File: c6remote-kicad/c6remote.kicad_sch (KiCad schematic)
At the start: 25 parts, among them J1 Battery, Q1 MMBT2222A, SW1 SW_Push, SW10 SW_Push, SW11 SW_Push, SW2 SW_Push, SW3 SW_Push, SW4 SW_Push, SW5 SW_Push, SW6 SW_Push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

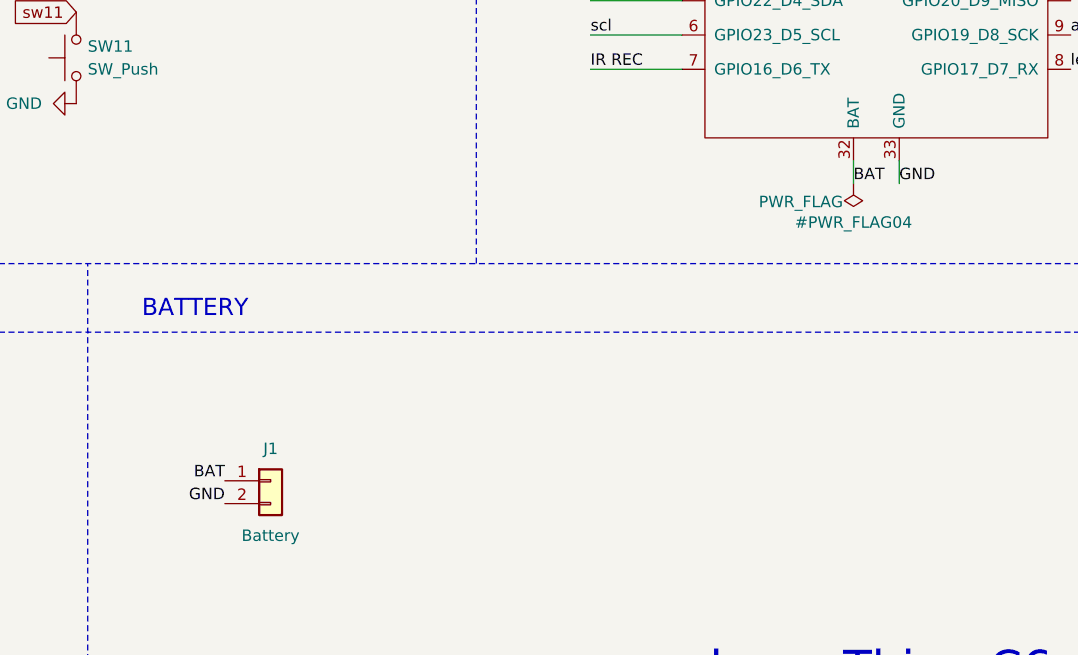
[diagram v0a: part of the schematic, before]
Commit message: fix(net): rename BAT local labels to global so net emits as 'BAT' not '/BAT'; patch stale PCB pad nets U1.32 BAT_32 and MK1.5 VDD_5 from PWR_FLAG to BAT/+3.3V; refill zones (DRC: 0 errors, 42 warnings, was 50 with 4 errors)
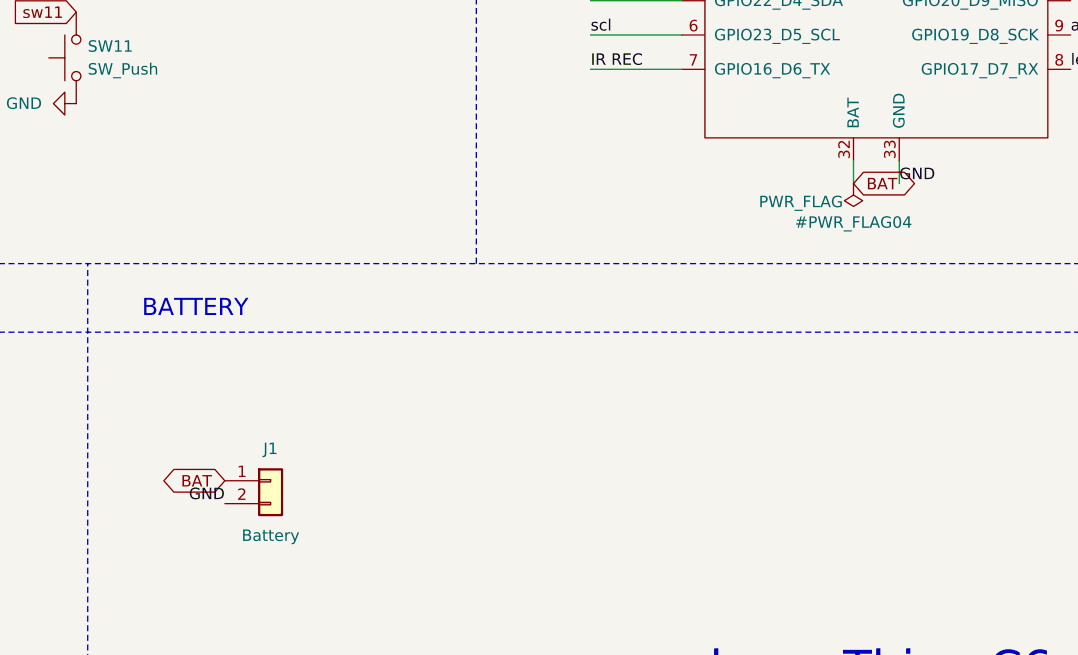
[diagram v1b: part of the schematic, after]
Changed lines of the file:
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@@
-		)
-	)
-	(label "BAT"
-		(at 128.27 153.67 180)
-		(effects
-			(font
-				(size 1.27 1.27)
-			)
-			(justify right bottom)
 		)
 	)
@@
 		)
 	)
-	(label "BAT"
-		(at 198.12 120.65 0)
-		(effects
-			(font
-				(size 1.27 1.27)
-			)
-			(justify left bottom)
-		)
-	)
 	(label "IR EMIT"
 		(at 168.91 88.9 0)
@@
 		)
 	)
+	(global_label "BAT"
+		(shape bidirectional)
+		(at 128.27 153.67 180)
+		(effects
+			(font
+				(size 1.27 1.27)
+			)
+			(justify right bottom)
+		)
+		(property "Intersheetrefs" "${INTERSHEET_REFS}"
+			(at 128.27 153.67 0)
+			(hide yes)
+			(show_name no)
+			(do_not_autoplace no)
+			(effects
+				(font
+					(size 1.27 1.27)
+				)
+			)
+		)
+	)
 	(global_label "ano_sw4"
 		(shape input)
@@
 			)
 		)
+	)
+	(global_label "BAT"
+		(shape bidirectional)
+		(at 198.12 120.65 0)
+		(effects
+			(font
+				(size 1.27 1.27)
+			)
+			(justify left bottom)
+		)
+		(property "Intersheetrefs" "${INTERSHEET_REFS}"
+			(at 198.12 120.65 0)
+			(hide yes)
+			(show_name no)
+			(do_not_autoplace no)
+			(effects
+				(font
+					(size 1.27 1.27)
+				)
+			)
+		)

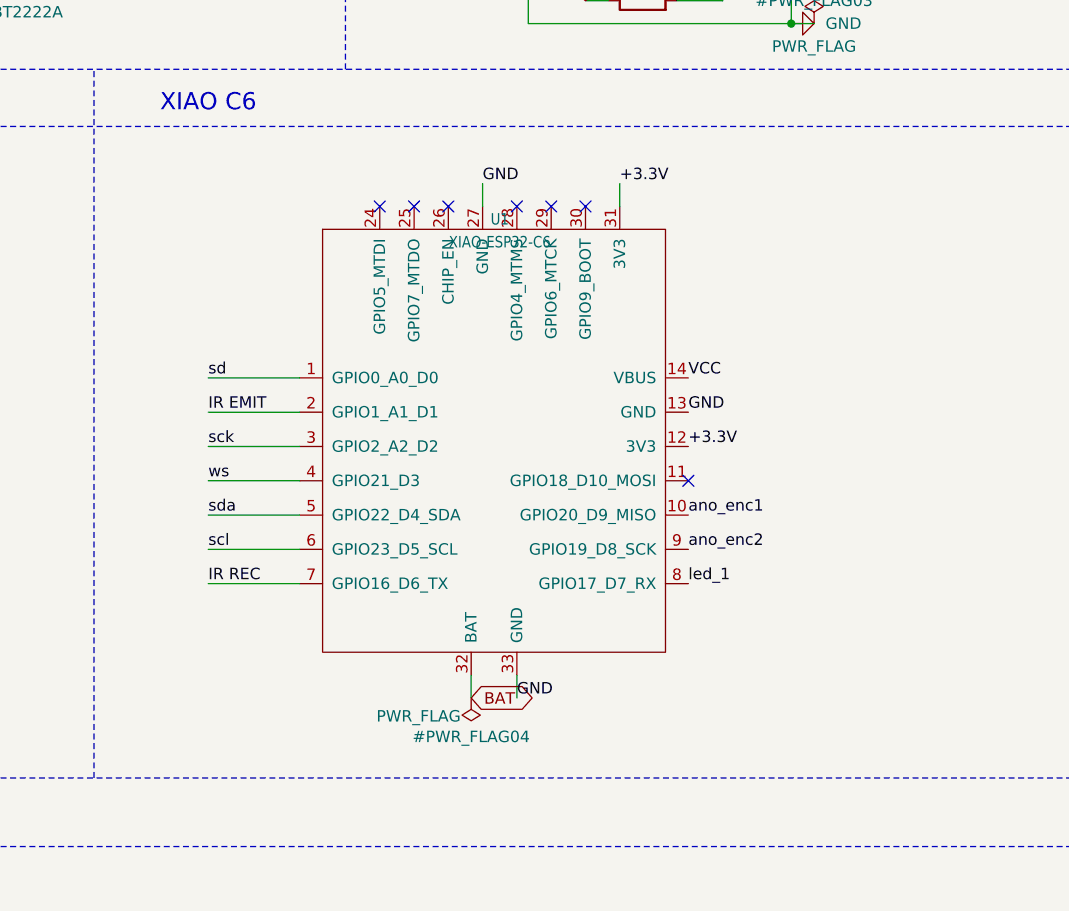
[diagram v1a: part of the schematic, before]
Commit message: feat(schematic): add I2C pull-ups R4 (4.7k SDA->+3.3V) and R5 (4.7k SCL->+3.3V) west of XIAO label bundle with shared #PWR033 +3.3V symbol; ERC clean (0 errors, 12 baseline warnings); PCB placement pending
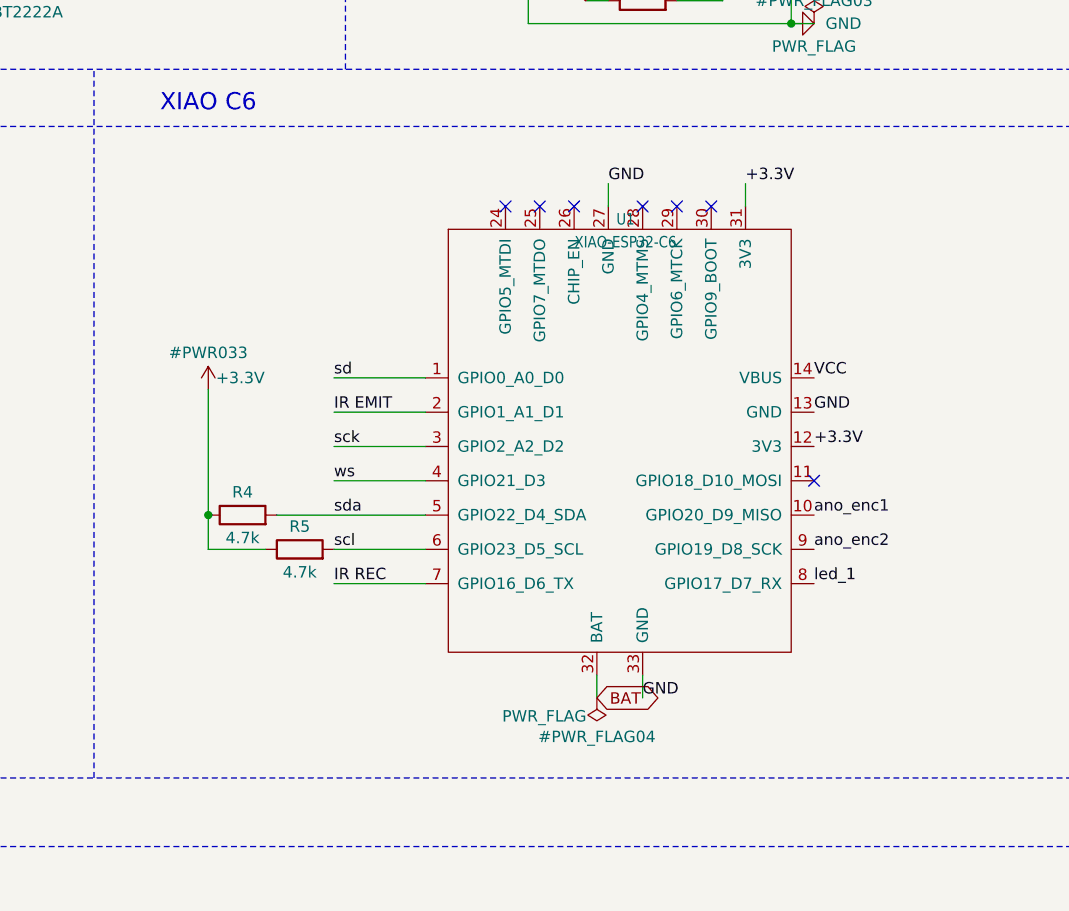
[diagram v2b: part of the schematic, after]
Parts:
- added R4, R5: 4.7k, Resistor_SMD:R_0603_1608Metric, symbol Device:R
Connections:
- net +3.3V: now also R4.1, R5.1
- net scl: now also R5.2
- net sda: now also R4.2
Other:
- moved on the sheet: U1

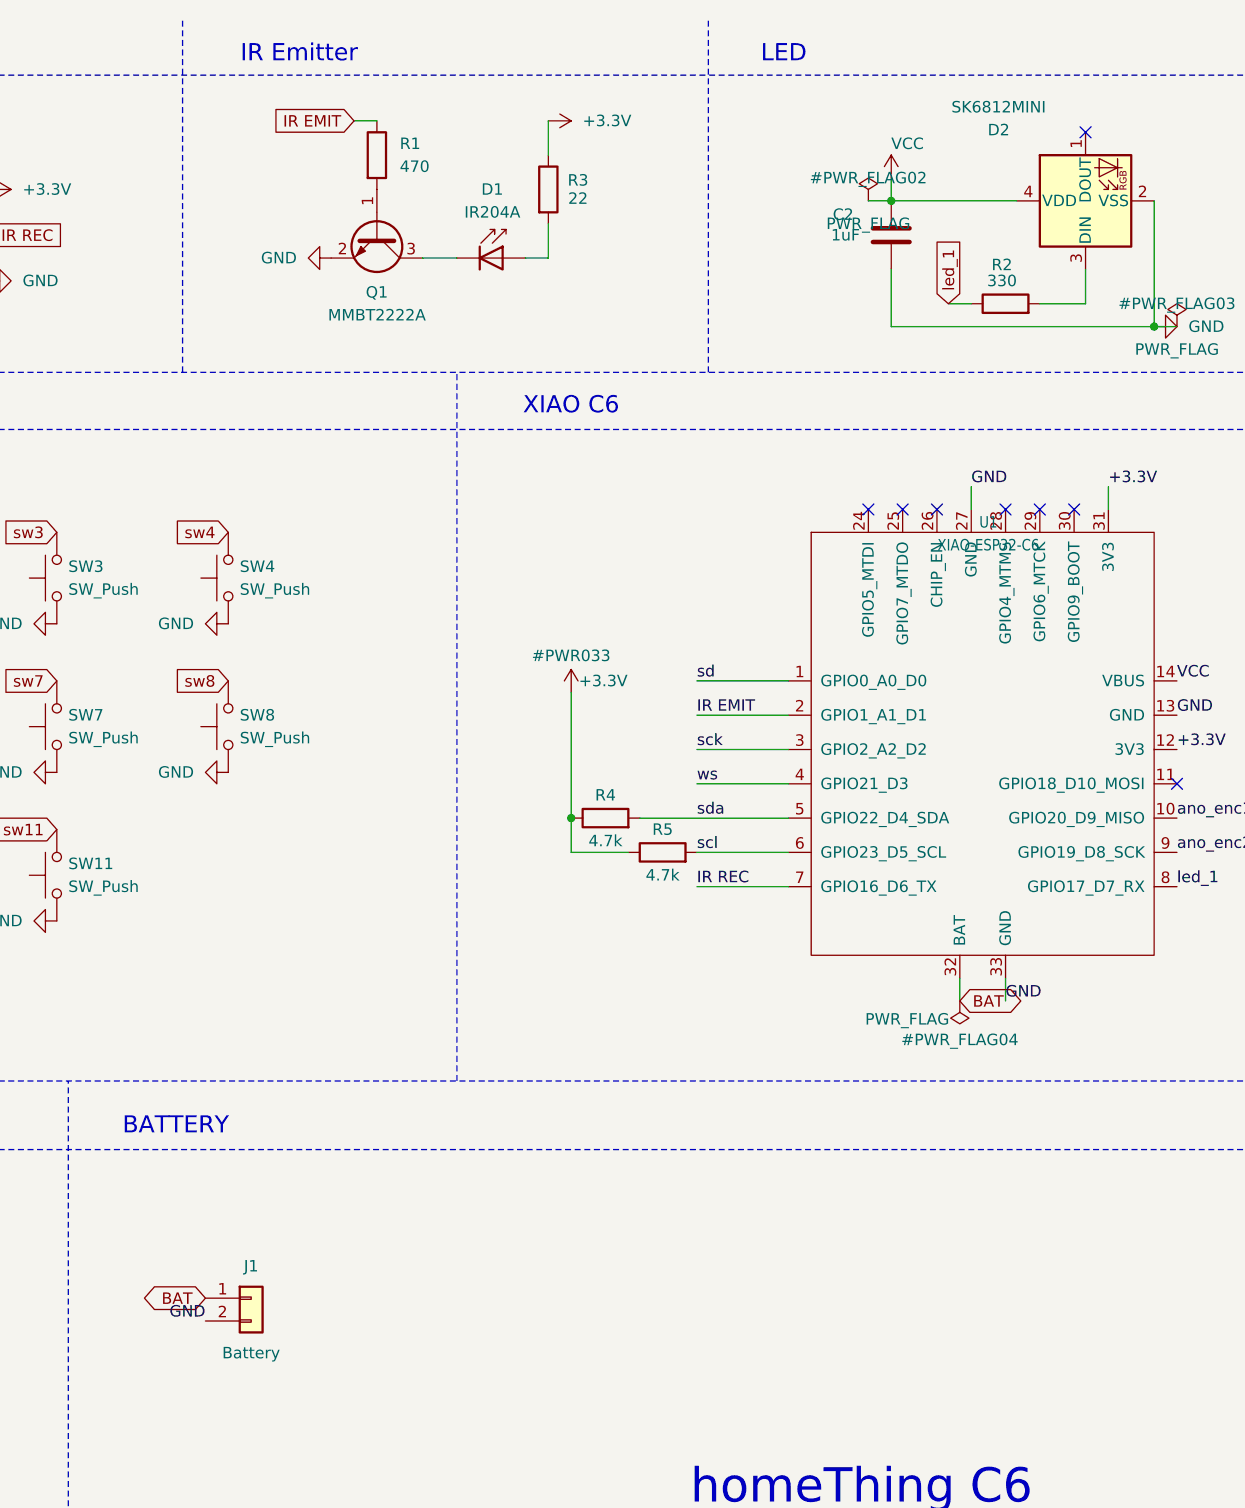
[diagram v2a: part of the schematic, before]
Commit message: fix(power): move SK6812 D2 supply from VCC (VBUS) to +3.3V so LED works on battery; rewires D2/4 + C2/1; VCC label now only U1/14 (orphan single-node /VCC net, rename to VBUS later)
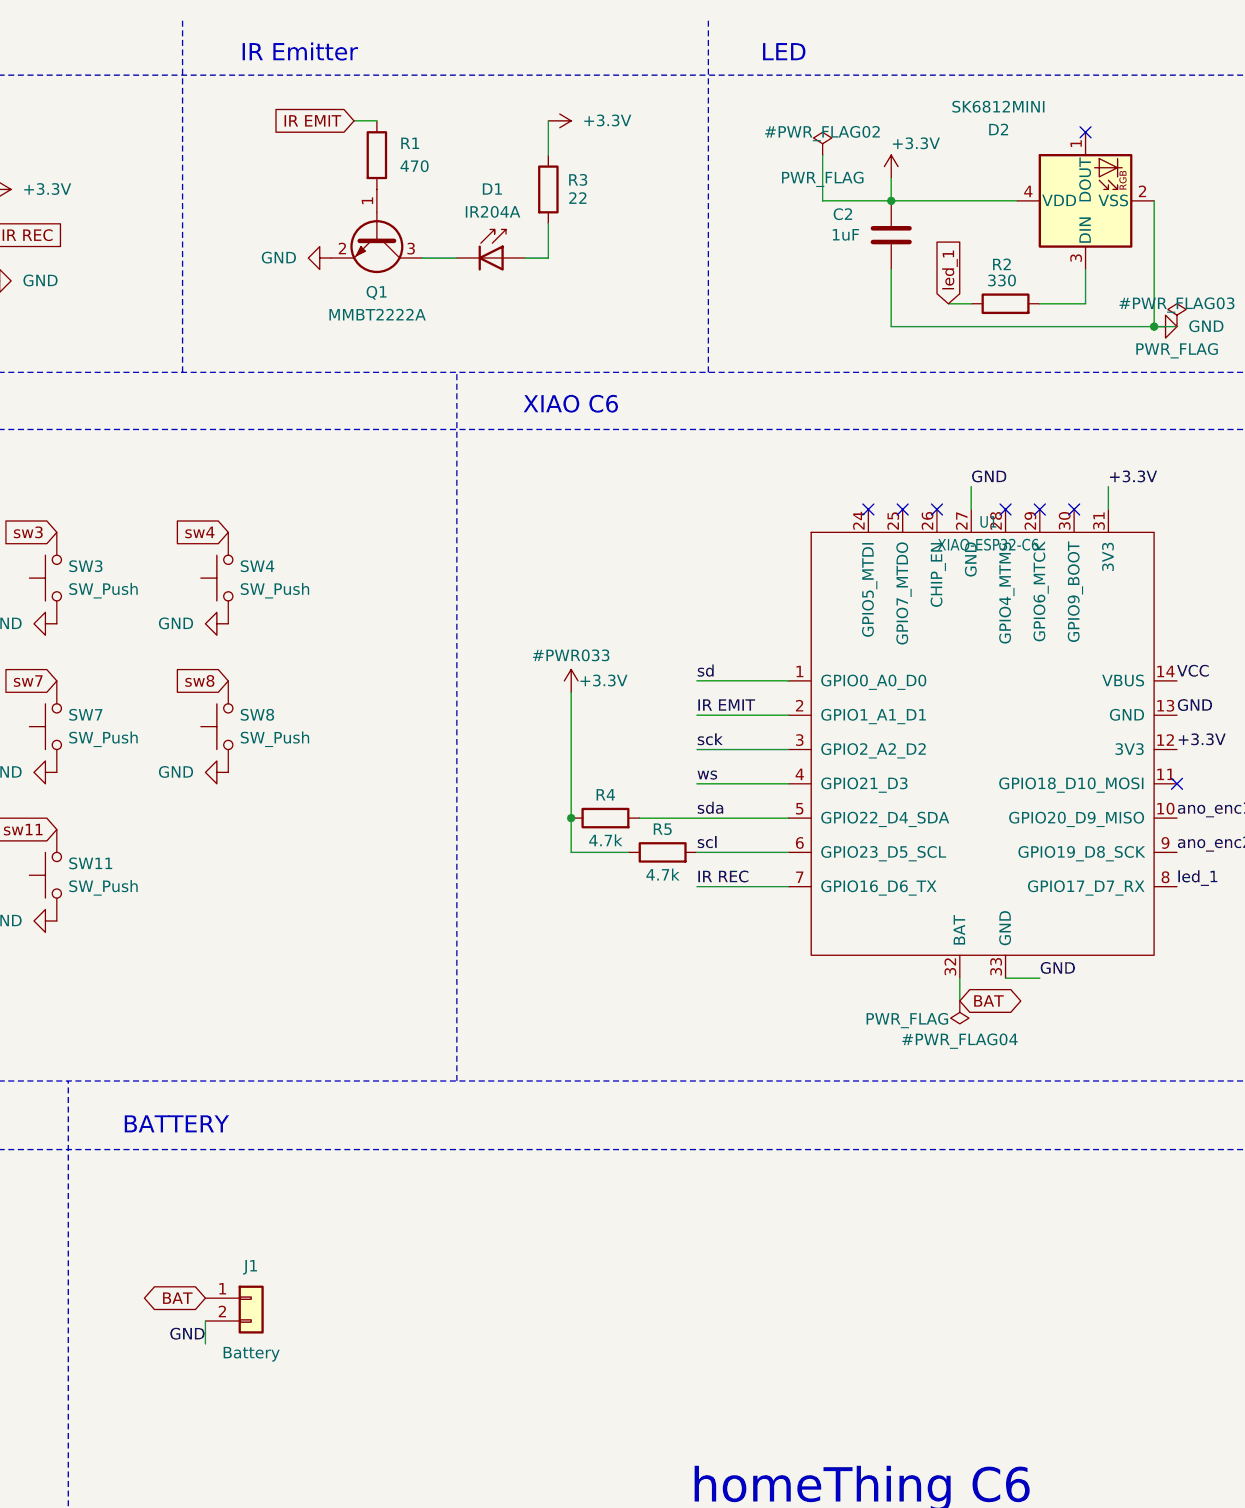
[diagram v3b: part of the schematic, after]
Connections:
- net +3.3V: now also C2.1, D2.4 (VDD)
- net VCC: no longer C2.1, D2.4 (VDD)
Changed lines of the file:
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@@
 	(wire
 		(pts
-			(xy 204.47 31.75) (xy 201.93 31.75)
-		)
-		(stroke
-			(width 0)
-			(type default)
-		)
-	)
-	(wire
-		(pts
 			(xy 20.32 119.38) (xy 41.91 119.38)
 		)
@@
 	(wire
 		(pts
+			(xy 196.85 26.67) (xy 196.85 31.75)
+		)
+		(stroke
+			(width 0)
+			(type default)
+		)
+	)
+	(wire
+		(pts
 			(xy 176.53 100.33) (xy 193.04 100.33)
 		)
@@
 	(wire
 		(pts
+			(xy 220.98 118.11) (xy 217.17 118.11)
+		)
+		(stroke
+			(width 0)
+			(type default)
+		)
+	)
+	(wire
+		(pts
 			(xy 228.6 66.04) (xy 228.6 63.5)
 		)
@@
 	(wire
 		(pts
+			(xy 128.27 158.75) (xy 128.27 156.21)
+		)
+		(stroke
+			(width 0)
+			(type default)
+		)
+	)
+	(wire
+		(pts
 			(xy 233.68 45.72) (xy 236.22 45.72)
 		)
@@
 		)
 	)
-	(wire
-		(pts
-			(xy 217.17 118.11) (xy 217.17 120.65)
-		)
-		(stroke
-			(width 0)
-			(type default)
-		)
-	)
 	(polyline
 		(pts
@@
 		)
 	)
+	(wire
+		(pts
+			(xy 196.85 31.75) (xy 204.47 31.75)
+		)
+		(stroke
+			(width 0)
+			(type default)
+		)
+	)
 	(label "ano_enc2"
 		(at 236.22 104.14 0)
@@
 	)
 	(label "GND"
-		(at 128.27 156.21 180)
+		(at 128.27 158.75 180)
 		(effects
 			(font
@@
 	)
 	(label "GND"
-		(at 217.17 120.65 0)
+		(at 220.98 118.11 0)
 		(effects
 			(font
@@
 	(symbol
 		(lib_id "power:PWR_FLAG")
-		(at 201.93 31.75 0)
+		(at 196.85 26.67 0)
 		(unit 1)
 		(body_style 1)
@@
 		(dnp no)
 		(property "Reference" "#PWR_FLAG02"
-			(at 201.93 29.21 0)
+			(at 196.85 24.13 0)
 			(show_name no)
 			(do_not_autoplace no)
@@
 		)
 		(property "Value" "PWR_FLAG"
-			(at 201.93 34.29 0)
+			(at 196.85 29.21 0)
 			(show_name no)
 			(do_not_autoplace no)
@@
 		)
 		(property "Footprint" ""
-			(at 201.93 31.75 0)
+			(at 196.85 26.67 0)
 			(hide yes)
 			(show_name no)
@@
 		)
 		(property "Datasheet" "~"
-			(at 201.93 31.75 0)
+			(at 196.85 26.67 0)
 			(hide yes)
 			(show_name no)
@@
 		)
 		(property "Description" ""
-			(at 201.93 31.75 0)
+			(at 196.85 26.67 0)
 			(show_name no)
 			(do_not_autoplace no)
@@
 	)
 	(symbol
-		(lib_id "power:VCC")
+		(lib_id "power:+3.3V")
 		(at 204.47 29.21 0)
 		(unit 1)
@@
 			)
 		)
-		(property "Value" "VCC"
+		(property "Value" "+3.3V"
 			(at 204.4699 25.4 0)
 			(show_name no)
@@
 			)
 		)
-		(property "Description" "Power symbol creates a global label with name \"VCC\""
+		(property "Description" "Power symbol creates a global label with name \"+3.3V\""
 			(at 204.47 29.21 0)
 			(hide yes)
